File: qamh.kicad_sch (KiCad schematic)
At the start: 17 parts

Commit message: pcb
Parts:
- added H1, H2: MountingHole, MountingHole:MountingHole_3.2mm_M3, symbol Mechanical:MountingHole
- RV1, RV2, RV3: renamed from RV?; footprint (none) -> Potentiometer_THT:Potentiometer_Alps_RK09K_Single_Vertical
- gave numbers to parts that had none: 14

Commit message: fix
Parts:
- removed H1, H2: MountingHole, MountingHole:MountingHole_3.2mm_M3, symbol Mechanical:MountingHole
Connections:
- net at D5.2 (A), D6.1 (K), J4.T: now also RV2.3; no longer RV2.2
- net at D1.2 (A), D2.1 (K), J3.T: now also RV1.3; no longer RV1.2
- net at A1.20 (A1): now also RV2.2; no longer RV2.3
- net at A1.21 (A2): now also RV1.2; no longer RV1.3
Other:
- moved on the sheet: J1

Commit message: fix (2) pot
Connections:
- net +5V: now also RV3.3; no longer RV3.2
- net at A1.19 (A0): now also RV3.2; no longer RV3.3
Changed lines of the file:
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@@
+    (stroke (width 0) (type default) (color 0 0 0 0))
+  )
+  (wire (pts (xy 190.5 97.79) (xy 190.5 101.6))
     (stroke (width 0) (type default) (color 0 0 0 0))
   )
@@
     (stroke (width 0) (type default) (color 0 0 0 0))
   )
+  (wire (pts (xy 161.29 97.79) (xy 190.5 97.79))
+    (stroke (width 0) (type default) (color 0 0 0 0))
+  )
   (wire (pts (xy 208.28 93.98) (xy 160.02 93.98))
     (stroke (width 0) (type default) (color 0 0 0 0))
   )
-  (wire (pts (xy 199.39 97.79) (xy 161.29 97.79))
+  (wire (pts (xy 190.5 101.6) (xy 195.58 101.6))
     (stroke (width 0) (type default) (color 0 0 0 0))
   )
@@
     (pin "1")
   )
+  (symbol (lib_id "power:+5V") (at 199.39 97.79 90) (unit 1)
+    (in_bom yes) (on_board yes) (fields_autoplaced)
+    (property "Reference" "#PWR?" (id 0) (at 203.2 97.79 0)
+      (effects (font (size 1.27 1.27)) hide)
+    )
+    (property "Value" "+5V" (id 1) (at 195.58 97.7899 90)
+      (effects (font (size 1.27 1.27)) (justify left))
+    )
+    (property "Footprint" "" (id 2) (at 199.39 97.79 0)
+      (effects (font (size 1.27 1.27)) hide)
+    )
+    (property "Datasheet" "" (id 3) (at 199.39 97.79 0)
+      (effects (font (size 1.27 1.27)) hide)
+    )
+    (pin "1")
+  )
   (symbol (lib_id "Device:R_Potentiometer") (at 199.39 83.82 180) (unit 1)
     (in_bom yes) (on_board yes) (fields_autoplaced)
@@
     (pin "1")
     (pin "2")
-  )
-  (symbol (lib_id "power:+5V") (at 195.58 101.6 90) (unit 1)
-    (in_bom yes) (on_board yes) (fields_autoplaced)
-    (property "Reference" "#PWR0111" (id 0) (at 199.39 101.6 0)
-      (effects (font (size 1.27 1.27)) hide)
-    )
-    (property "Value" "+5V" (id 1) (at 191.77 101.5999 90)
-      (effects (font (size 1.27 1.27)) (justify left))
-    )
-    (property "Footprint" "" (id 2) (at 195.58 101.6 0)
-      (effects (font (size 1.27 1.27)) hide)
-    )
-    (property "Datasheet" "" (id 3) (at 195.58 101.6 0)
-      (effects (font (size 1.27 1.27)) hide)
-    )
-    (pin "1")
   )
   (symbol (lib_id "Device:R") (at 113.03 92.71 90) (unit 1)
@@
       (reference "#PWR0110") (unit 1) (value "GND") (footprint "")
     )
-    (path "/c0c305dd-8022-4177-bf91-5e10f3fd8b11"
-      (reference "#PWR0111") (unit 1) (value "+5V") (footprint "")
-    )
     (path "/aa776419-3690-4c63-aaa9-dd5ddfc25891"
       (reference "#PWR0112") (unit 1) (value "GND") (footprint "")
@@
       (reference "#PWR0125") (unit 1) (value "GND") (footprint "")
     )
+    (path "/6bac5099-cded-49d1-a037-2bdbe58b2a0e"
+      (reference "#PWR?") (unit 1) (value "+5V") (footprint "")
+    )
     (path "/c8475a3e-bf66-487a-a33c-f2518f94c497"

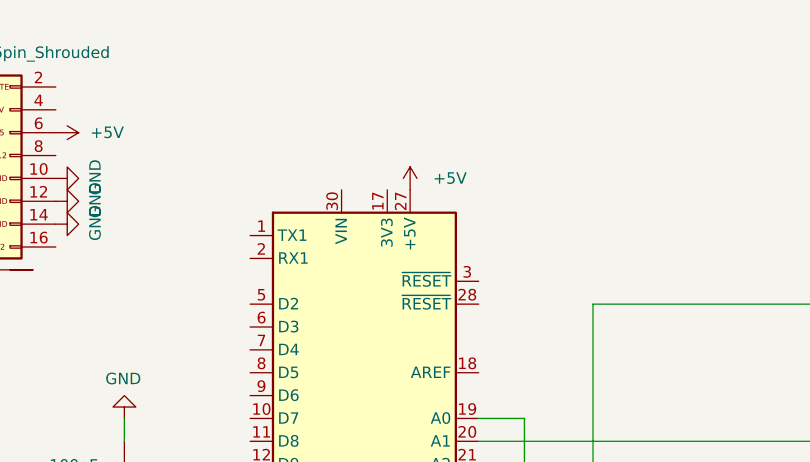
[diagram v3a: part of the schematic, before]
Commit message: power needs to be fed via the vin of the nano
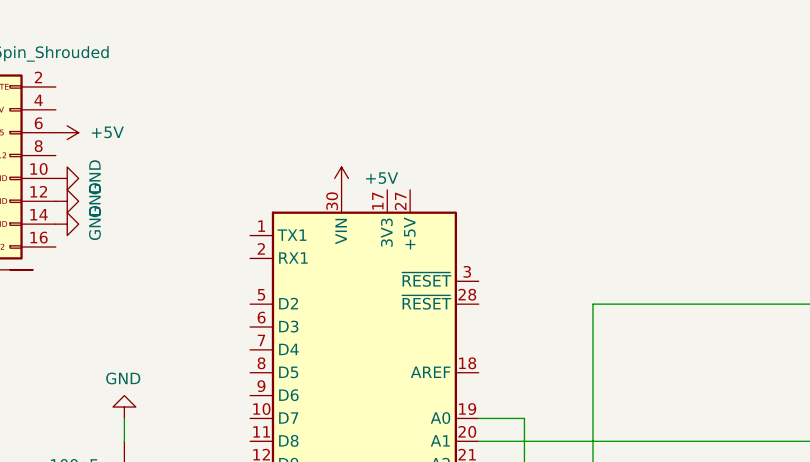
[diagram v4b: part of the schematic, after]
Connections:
- net +5V: now also A1.30 (VIN); no longer A1.27 (+5V)

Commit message: logo's, header for piezo
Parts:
- added J6: Conn_01x02_Pin, Connector_PinHeader_2.54mm:PinHeader_1x02_P2.54mm_Vertical, symbol Connector:Conn_01x02_Pin
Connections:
- net GND: now also J6.1 (Pin_1)
- net at A1.9 (D6): now also J6.2 (Pin_2)
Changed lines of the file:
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@@
+    (stroke (width 0) (type default))
+  )
+  (wire (pts (xy 120.65 77.47) (xy 130.81 77.47))
     (stroke (width 0) (type default))
   )
@@
     (stroke (width 0) (type default))
   )
+  (wire (pts (xy 120.65 72.39) (xy 120.65 77.47))
+    (stroke (width 0) (type default))
+  )
   (wire (pts (xy 168.91 85.09) (xy 156.21 85.09))
     (stroke (width 0) (type default))
@@
   )
   (wire (pts (xy 199.39 80.01) (xy 214.63 80.01))
+    (stroke (width 0) (type default))
+  )
+  (wire (pts (xy 73.66 72.39) (xy 120.65 72.39))
     (stroke (width 0) (type default))
   )
@@
         (path "/c13d4df3-e81e-4244-a624-8f3edbb92138"
           (reference "RV1") (unit 1)
+        )
+      )
+    )
+  )
+  (symbol (lib_id "power:GND") (at 73.66 69.85 90) (unit 1)
+    (in_bom yes) (on_board yes) (dnp no)
+    (property "Reference" "#PWR02" (at 80.01 69.85 0)
+      (effects (font (size 1.27 1.27)) hide)
+    )
+    (property "Value" "GND" (at 78.0542 69.723 0)
+      (effects (font (size 1.27 1.27)))
+    )
+    (property "Footprint" "" (at 73.66 69.85 0)
+      (effects (font (size 1.27 1.27)) hide)
+    )
+    (property "Datasheet" "" (at 73.66 69.85 0)
+      (effects (font (size 1.27 1.27)) hide)
+    )
+    (pin "1")
+    (instances
+      (project "qamh"
+        (path "/c13d4df3-e81e-4244-a624-8f3edbb92138"
+          (reference "#PWR02") (unit 1)
         )
       )
@@
         )
       )
+    )
+  )
+  (symbol (lib_id "Connector:Conn_01x02_Pin") (at 68.58 69.85 0) (unit 1)
+    (in_bom yes) (on_board yes) (dnp no) (fields_autoplaced)
+    (property "Reference" "J6" (at 69.215 64.77 0)
+      (effects (font (size 1.27 1.27)))
+    )
+    (property "Value" "Conn_01x02_Pin" (at 69.215 67.31 0)
+      (effects (font (size 1.27 1.27)))
+    )
+    (property "Footprint" "Connector_PinHeader_2.54mm:PinHeader_1x02_P2.54mm_Vertical" (at 68.58 69.85 0)
+      (effects (font (size 1.27 1.27)) hide)
+    )
+    (property "Datasheet" "~" (at 68.58 69.85 0)
+      (effects (font (size 1.27 1.27)) hide)
+    )
+    (pin "1")
+    (pin "2")
+    (instances
+      (project "qamh"
+        (path "/c13d4df3-e81e-4244-a624-8f3edbb92138"
+          (reference "J6") (unit 1)
+        )
+      )

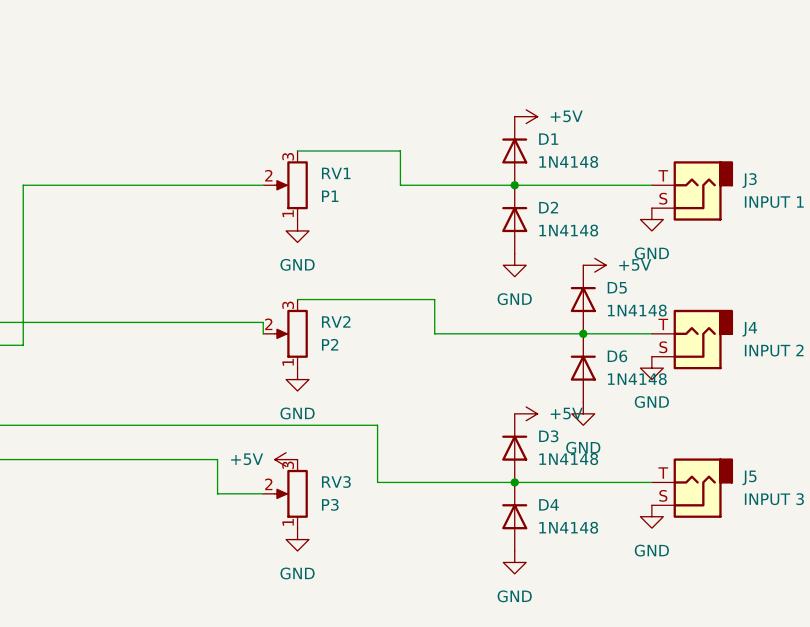
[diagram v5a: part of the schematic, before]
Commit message: potmeters are B10k (linear 10k ohm)
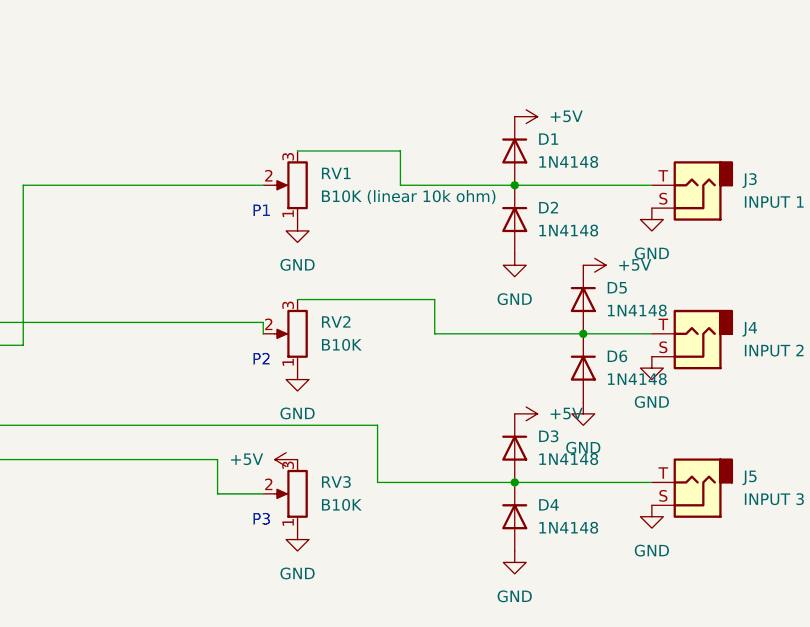
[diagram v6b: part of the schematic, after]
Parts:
- RV1: value P1 -> B10K (linear 10k ohm)
- RV2: value P2 -> B10K
- RV3: value P3 -> B10K
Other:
- note added: "P1"
- note added: "P2"
- note added: "P3"
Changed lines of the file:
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@@
     (stroke (width 0) (type default))
+  )
+  (text "P2" (at 194.31 87.63 0)
+    (effects (font (size 1.27 1.27)) (justify left bottom))
+  )
+  (text "P1" (at 194.31 71.12 0)
+    (effects (font (size 1.27 1.27)) (justify left bottom))
+  )
+  (text "P3" (at 194.31 105.41 0)
+    (effects (font (size 1.27 1.27)) (justify left bottom))
   )
   (symbol (lib_id "Diode:1N4148") (at 223.52 96.52 270) (unit 1)
@@
   (symbol (lib_id "Device:R_Potentiometer") (at 199.39 83.82 180) (unit 1)
     (in_bom yes) (on_board yes) (dnp no) (fields_autoplaced)
-    (property "Reference" "RV2" (at 201.93 82.5499 0)
-      (effects (font (size 1.27 1.27)) (justify right))
-    )
-    (property "Value" "P2" (at 201.93 85.0899 0)
+    (property "Reference" "RV2" (at 201.93 82.55 0)
+      (effects (font (size 1.27 1.27)) (justify right))
+    )
+    (property "Value" "B10K" (at 201.93 85.09 0)
       (effects (font (size 1.27 1.27)) (justify right))
     )
@@
   (symbol (lib_id "Device:R_Potentiometer") (at 199.39 67.31 180) (unit 1)
     (in_bom yes) (on_board yes) (dnp no) (fields_autoplaced)
-    (property "Reference" "RV1" (at 201.93 66.0399 0)
-      (effects (font (size 1.27 1.27)) (justify right))
-    )
-    (property "Value" "P1" (at 201.93 68.5799 0)
+    (property "Reference" "RV1" (at 201.93 66.04 0)
+      (effects (font (size 1.27 1.27)) (justify right))
+    )
+    (property "Value" "B10K (linear 10k ohm)" (at 201.93 68.58 0)
       (effects (font (size 1.27 1.27)) (justify right))
     )
@@
   (symbol (lib_id "Device:R_Potentiometer") (at 199.39 101.6 180) (unit 1)
     (in_bom yes) (on_board yes) (dnp no) (fields_autoplaced)
-    (property "Reference" "RV3" (at 201.93 100.3299 0)
-      (effects (font (size 1.27 1.27)) (justify right))
-    )
-    (property "Value" "P3" (at 201.93 102.8699 0)
-      (effects (font (size 1.27 1.27)) (justify right))
-    )
+    (property "Reference" "RV3" (at 201.93 100.33 0)
+      (effects (font (size 1.27 1.27)) (justify right))
+    )
+    (property "Value" "B10K" (at 201.93 102.87 0)
+      (effects (font (size 1.27 1.27)) (justify right))
+    )

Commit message: meta data in sheet
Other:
- company: (none) -> www.vanheusden.com
- title: (none) -> Qamh
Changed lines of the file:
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@@
 (kicad_sch (version 20230121) (generator eeschema)
   (paper "A4")
+  (title_block
+    (title "Qamh")
+    (date "2023-10-07")
+    (rev "0.1")
+    (company "www.vanheusden.com")
+    (comment 1 "https://github.com/folkertvanheusden/qamh/")
+  )
   (junction (at 223.52 100.33) (diameter 0) (color 0 0 0 0)
   )

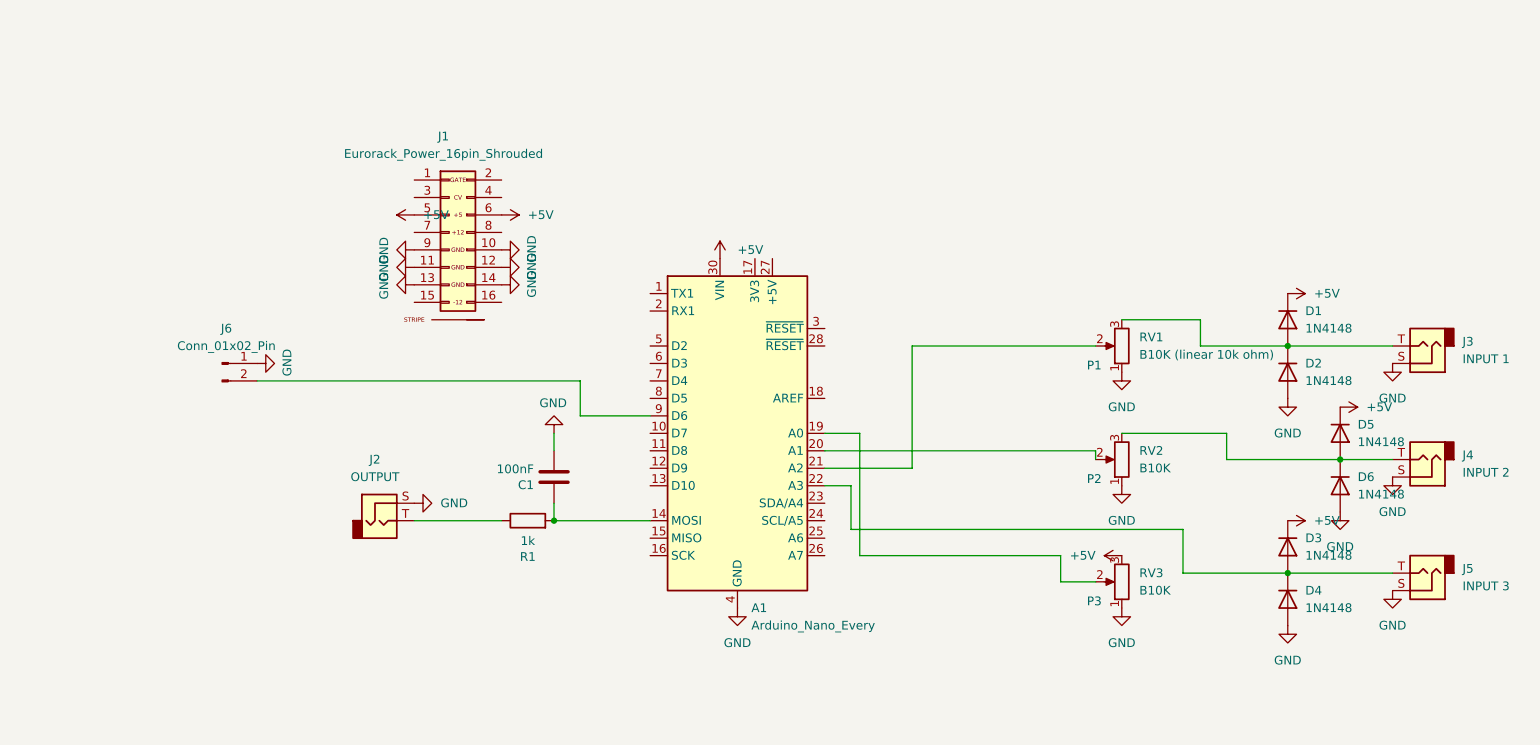
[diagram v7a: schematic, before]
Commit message: added button to D2
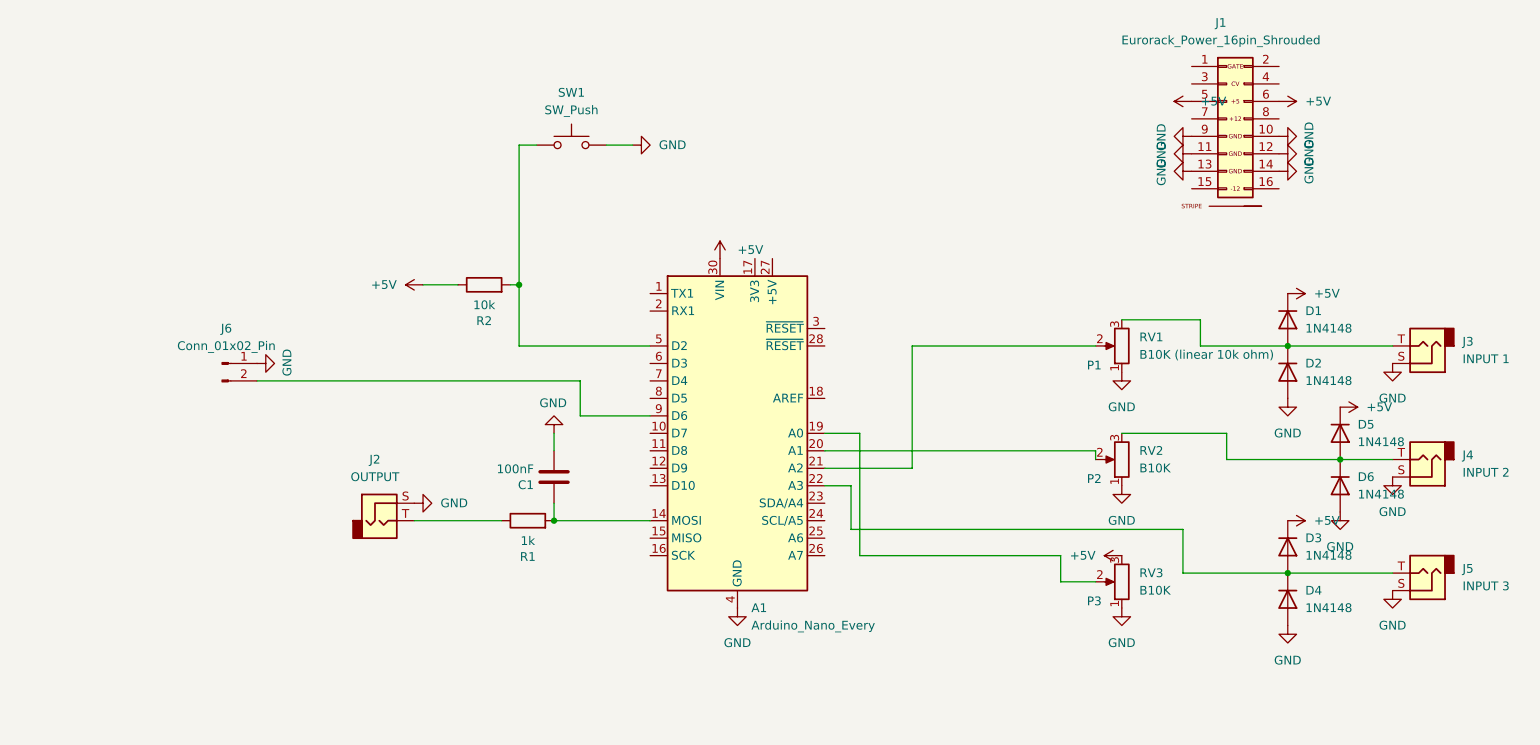
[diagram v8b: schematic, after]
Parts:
- added R2: 10k, Resistor_THT:R_Axial_DIN0204_L3.6mm_D1.6mm_P7.62mm_Horizontal, symbol Device:R
- added SW1: SW_Push, Button_Switch_THT:SW_PUSH_6mm_H5mm, symbol Switch:SW_Push
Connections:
- net +5V: now also R2.1
- net GND: now also SW1.2
- net at A1.5 (D2): now also R2.2, SW1.1
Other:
- moved on the sheet: J1
